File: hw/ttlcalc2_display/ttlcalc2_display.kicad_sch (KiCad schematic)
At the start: 25 parts, among them J1 DISP_CONN, J2 IO_BUS, Q1 MPSA42, Q2 MPSA42, Q3 MPSA42, Q4 MPSA42, U1 74LS138, U10 74LS04, U19 74LS04, U2 74LS138, U3 74LS173, U4 74LS173, U5 74LS173, U6 74LS08, U7 74LS173

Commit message: Display driver geographical reannotate
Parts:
- renumbered H6 to H4, H4 to H6, J2 to J4, Q2 to Q1, Q1 to Q10, Q4 to Q11, Q3 to Q24, R2 to R15, R4 to R16, R1 to R35, R3 to R36, U3 to U1, U19 to U13, U1 to U16, U6 to U17, U7 to U18, U4 to U19, U5 to U4, U10 to U5, U2 to U9
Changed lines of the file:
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@@
 		(dnp no)
 		(fields_autoplaced yes)
-		(property "Reference" "U7"
+		(property "Reference" "U18"
 			(at 270.1641 118.11 0)
 			(effects
@@
 			(project "ttlcalc2_display"
 				(path "/4da693c8-a60c-4d11-a405-739e88984bfc"
-					(reference "U7")
+					(reference "U18")
 					(unit 1)
 				)
@@
 		(dnp no)
 		(fields_autoplaced yes)
-		(property "Reference" "U3"
+		(property "Reference" "U1"
 			(at 169.8341 26.67 0)
 			(effects
@@
 			(project "ttlcalc2_display"
 				(path "/4da693c8-a60c-4d11-a405-739e88984bfc"
-					(reference "U3")
+					(reference "U1")
 					(unit 1)
 				)
@@
 		(dnp no)
 		(fields_autoplaced yes)
-		(property "Reference" "U6"
+		(property "Reference" "U17"
 			(at 245.1017 44.45 0)
 			(effects
@@
 			(project ""
 				(path "/4da693c8-a60c-4d11-a405-739e88984bfc"
-					(reference "U6")
+					(reference "U17")
 					(unit 1)
 				)
@@
 		(dnp no)
 		(fields_autoplaced yes)
-		(property "Reference" "U19"
+		(property "Reference" "U13"
 			(at 78.74 220.98 0)
 			(effects
@@
 			(project "ttlcalc2_display"
 				(path "/4da693c8-a60c-4d11-a405-739e88984bfc"
-					(reference "U19")
+					(reference "U13")
 					(unit 4)
 				)
@@
 		(dnp no)
 		(fields_autoplaced yes)
-		(property "Reference" "R4"
+		(property "Reference" "R16"
 			(at 280.67 227.33 90)
 			(effects
@@
 			(project "ttlcalc2_display"
 				(path "/4da693c8-a60c-4d11-a405-739e88984bfc"
-					(reference "R4")
+					(reference "R16")
 					(unit 1)
 				)
@@
 		(dnp no)
 		(fields_autoplaced yes)
-		(property "Reference" "R2"
+		(property "Reference" "R15"
 			(at 280.67 186.69 90)
 			(effects
@@
 			(project "ttlcalc2_display"
 				(path "/4da693c8-a60c-4d11-a405-739e88984bfc"
-					(reference "R2")
+					(reference "R15")
 					(unit 1)
 				)
@@
 		(dnp no)
 		(fields_autoplaced yes)
-		(property "Reference" "U2"
+		(property "Reference" "U9"
 			(at 111.4141 133.35 0)
 			(effects
@@
 			(project "ttlcalc2_display"
 				(path "/4da693c8-a60c-4d11-a405-739e88984bfc"
-					(reference "U2")
+					(reference "U9")
 					(unit 1)
 				)
@@
 		(dnp no)
 		(fields_autoplaced yes)
-		(property "Reference" "U6"
+		(property "Reference" "U17"
 			(at 383.5317 193.04 0)
 			(effects
@@
 			(project "ttlcalc2_display"
 				(path "/4da693c8-a60c-4d11-a405-739e88984bfc"
-					(reference "U6")
+					(reference "U17")
 					(unit 4)
 				)
@@
 		(dnp no)
 		(fields_autoplaced yes)
-		(property "Reference" "U10"
+		(property "Reference" "U5"
 			(at 45.72 220.98 0)
 			(effects
@@
 			(project "ttlcalc2_display"
 				(path "/4da693c8-a60c-4d11-a405-739e88984bfc"
-					(reference "U10")
+					(reference "U5")
 					(unit 6)
 				)
@@
 		(dnp no)
 		(fields_autoplaced yes)
-		(property "Reference" "Q2"
+		(property "Reference" "Q1"
 			(at 295.91 191.7699 0)
 			(effects
@@
 			(project "ttlcalc2_display"
 				(path "/4da693c8-a60c-4d11-a405-739e88984bfc"
-					(reference "Q2")
+					(reference "Q1")
 					(unit 1)
 				)
@@
 		(dnp no)
 		(fields_autoplaced yes)
-		(property "Reference" "U1"
+		(property "Reference" "U16"
 			(at 51.7241 133.35 0)
 			(effects
@@
 			(project "ttlcalc2_display"
 				(path "/4da693c8-a60c-4d11-a405-739e88984bfc"
-					(reference "U1")
+					(reference "U16")
 					(unit 1)
 				)
@@
 		(dnp no)
 		(fields_autoplaced yes)
-		(property "Reference" "U19"
+		(property "Reference" "U13"
 			(at 78.74 205.74 0)
 			(effects
@@
 			(project "ttlcalc2_display"
 				(path "/4da693c8-a60c-4d11-a405-739e88984bfc"
-					(reference "U19")
+					(reference "U13")
 					(unit 3)
 				)
@@
 		(dnp no)
 		(fields_autoplaced yes)
-		(property "Reference" "U6"
+		(property "Reference" "U17"
 			(at 245.1017 59.69 0)
 			(effects
@@
 			(project ""
 				(path "/4da693c8-a60c-4d11-a405-739e88984bfc"
-					(reference "U6")
+					(reference "U17")
 					(unit 2)
 				)
@@
 		(dnp no)
 		(fields_autoplaced yes)
-		(property "Reference" "U10"
+		(property "Reference" "U5"
 			(at 45.72 205.74 0)
 			(effects
@@
 			(project "ttlcalc2_display"
 				(path "/4da693c8-a60c-4d11-a405-739e88984bfc"
-					(reference "U10")
+					(reference "U5")
 					(unit 5)
 				)
@@
 		(dnp no)
 		(fields_autoplaced yes)
-		(property "Reference" "Q3"
+		(property "Reference" "Q24"
 			(at 295.91 212.0899 0)
 			(effects
@@
 			(project "ttlcalc2_display"
 				(path "/4da693c8-a60c-4d11-a405-739e88984bfc"
-					(reference "Q3")
+					(reference "Q24")
 					(unit 1)
 				)
@@
 		(dnp no)
 		(fields_autoplaced yes)
-		(property "Reference" "U5"
+		(property "Reference" "U4"
 			(at 219.3641 182.88 0)
 			(effects
@@
 			(project "ttlcalc2_display"
 				(path "/4da693c8-a60c-4d11-a405-739e88984bfc"
-					(reference "U5")
+					(reference "U4")
 					(unit 1)
 				)
@@
 		(dnp no)
 		(fields_autoplaced yes)
-		(property "Reference" "Q4"
+		(property "Reference" "Q11"
 			(at 295.91 232.4099 0)
 			(effects
@@
 			(project "ttlcalc2_display"
 				(path "/4da693c8-a60c-4d11-a405-739e88984bfc"
-					(reference "Q4")
+					(reference "Q11")
 					(unit 1)
 				)
@@
 		(dnp no)
 		(fields_autoplaced yes)
-		(property "Reference" "H4"
+		(property "Reference" "H6"
 			(at 271.78 251.4599 0)
 			(effects
@@
 			(project "ttlcalc2_display"
 				(path "/4da693c8-a60c-4d11-a405-739e88984bfc"
-					(reference "H4")
+					(reference "H6")
 					(unit 1)
 				)
@@
 		(dnp no)
 		(fields_autoplaced yes)
-		(property "Reference" "J2"
+		(property "Reference" "J4"
 			(at 355.6 172.72 0)
 			(effects
@@
 			(project "ttlcalc2_display"
 				(path "/4da693c8-a60c-4d11-a405-739e88984bfc"
-					(reference "J2")
+					(reference "J4")
 					(unit 1)
 				)
@@
 		(dnp no)
 		(fields_autoplaced yes)
-		(property "Reference" "U19"
+		(property "Reference" "U13"
 			(at 106.68 220.98 0)
 			(effects
@@
 			(project "ttlcalc2_display"
 				(path "/4da693c8-a60c-4d11-a405-739e88984bfc"
-					(reference "U19")
+					(reference "U13")
 					(unit 6)
 				)
@@
 		(dnp no)
 		(fields_autoplaced yes)
-		(property "Reference" "U19"
+		(property "Reference" "U13"
 			(at 106.68 205.74 0)
 			(effects
@@
 			(project "ttlcalc2_display"
 				(path "/4da693c8-a60c-4d11-a405-739e88984bfc"
-					(reference "U19")
+					(reference "U13")
 					(unit 5)
 				)
@@
 		(dnp no)
 		(fields_autoplaced yes)
-		(property "Reference" "U4"
+		(property "Reference" "U19"
 			(at 218.0941 74.93 0)
 			(effects
@@
 			(project "ttlcalc2_display"
 				(path "/4da693c8-a60c-4d11-a405-739e88984bfc"
-					(reference "U4")
+					(reference "U19")
 					(unit 1)
 				)
@@
 		(dnp no)
 		(fields_autoplaced yes)
-		(property "Reference" "R1"
+		(property "Reference" "R35"
 			(at 280.67 166.37 90)
 			(effects
@@
 			(project "ttlcalc2_display"
 				(path "/4da693c8-a60c-4d11-a405-739e88984bfc"
-					(reference "R1")
+					(reference "R35")
 					(unit 1)
 				)
@@
 		(dnp no)
 		(fields_autoplaced yes)
-		(property "Reference" "H6"
+		(property "Reference" "H4"
 			(at 290.83 251.4599 0)
 			(effects
@@
 			(project "ttlcalc2_display"
 				(path "/4da693c8-a60c-4d11-a405-739e88984bfc"
-					(reference "H6")
+					(reference "H4")
 					(unit 1)
 				)
@@
 		(dnp no)
 		(fields_autoplaced yes)
-		(property "Reference" "U6"
+		(property "Reference" "U17"
 			(at 264.1517 52.07 0)
 			(effects
@@
 			(project ""
 				(path "/4da693c8-a60c-4d11-a405-739e88984bfc"
-					(reference "U6")
+					(reference "U17")
 					(unit 3)
 				)
@@
 		(dnp no)
 		(fields_autoplaced yes)
-		(property "Reference" "Q1"
+		(property "Reference" "Q10"
 			(at 295.91 171.4499 0)
 			(effects
@@
 			(project "ttlcalc2_display"
 				(path "/4da693c8-a60c-4d11-a405-739e88984bfc"
-					(reference "Q1")
+					(reference "Q10")
 					(unit 1)
 				)
@@
 		(dnp no)
 		(fields_autoplaced yes)
-		(property "Reference" "R3"
+		(property "Reference" "R36"
 			(at 280.67 207.01 90)
 			(effects
@@
 			(project "ttlcalc2_display"
 				(path "/4da693c8-a60c-4d11-a405-739e88984bfc"
-					(reference "R3")
+					(reference "R36")
 					(unit 1)
 				)

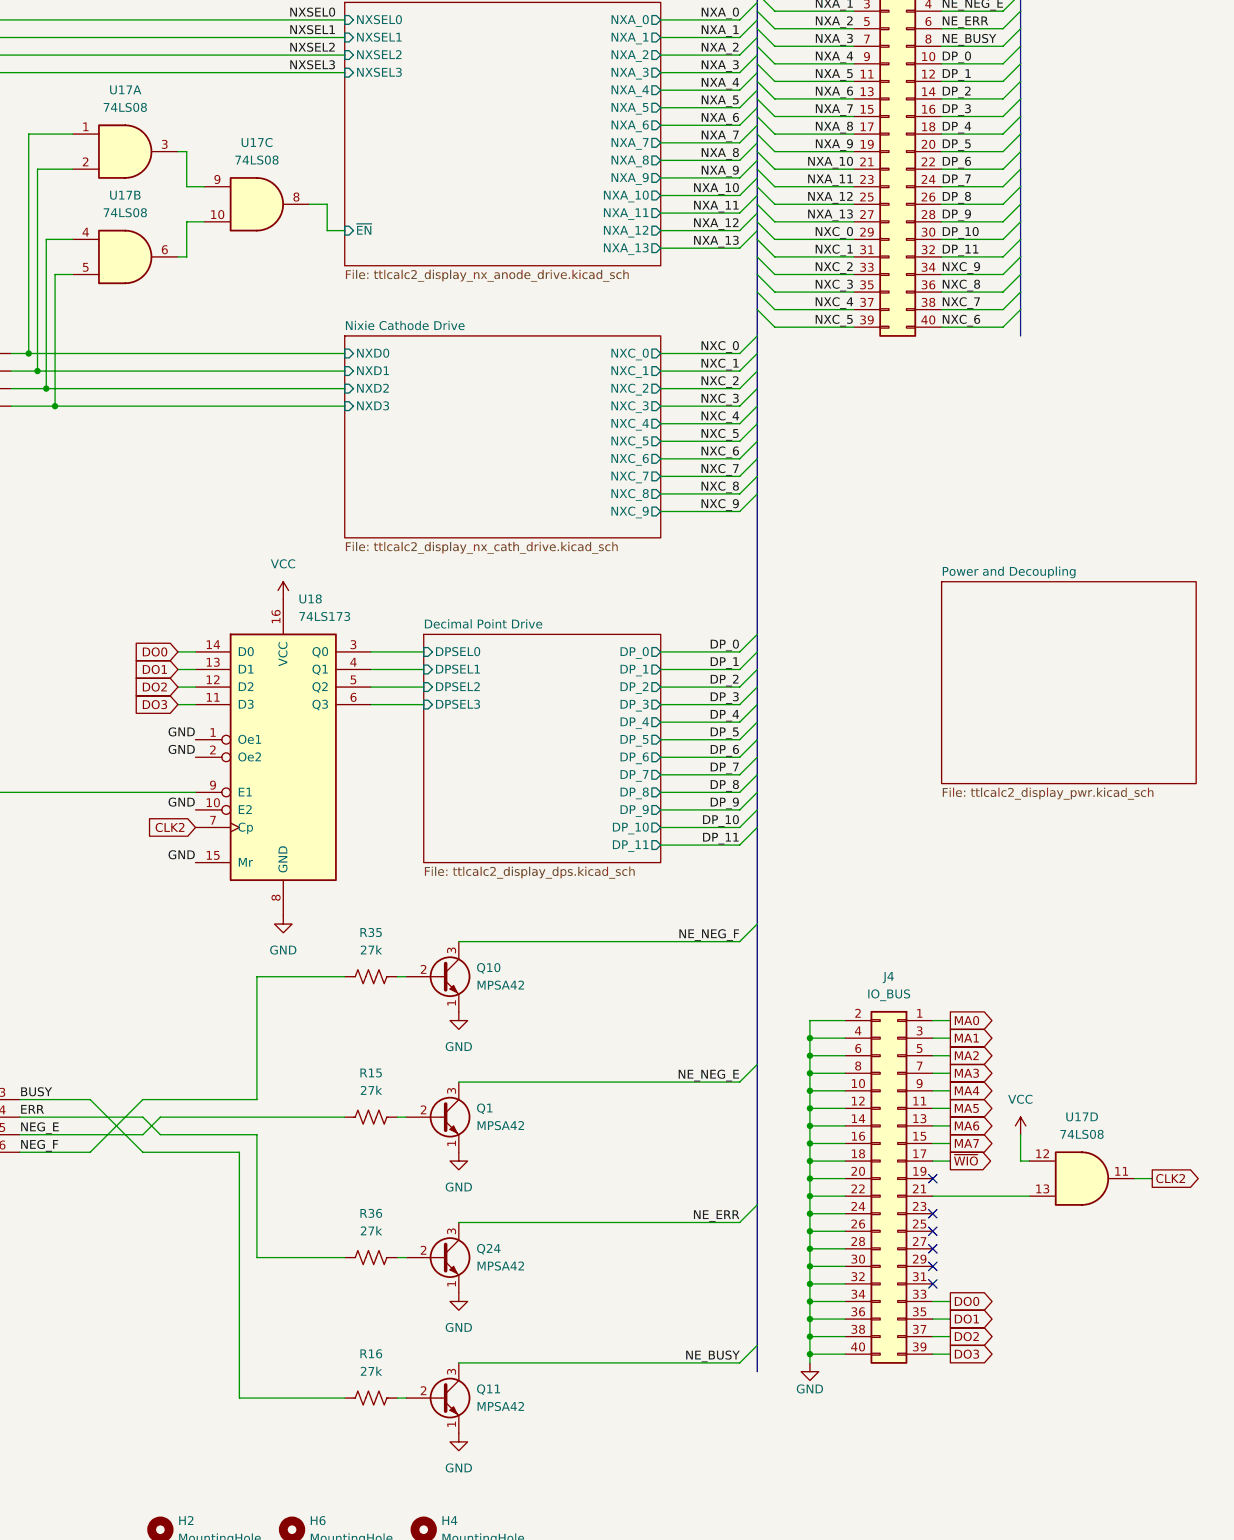
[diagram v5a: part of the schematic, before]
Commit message: Convert to KiCad 9.0
Convert to KiCad 9.0 format
Tweak silkscreen to fix DRC errors introduced by updated footprints
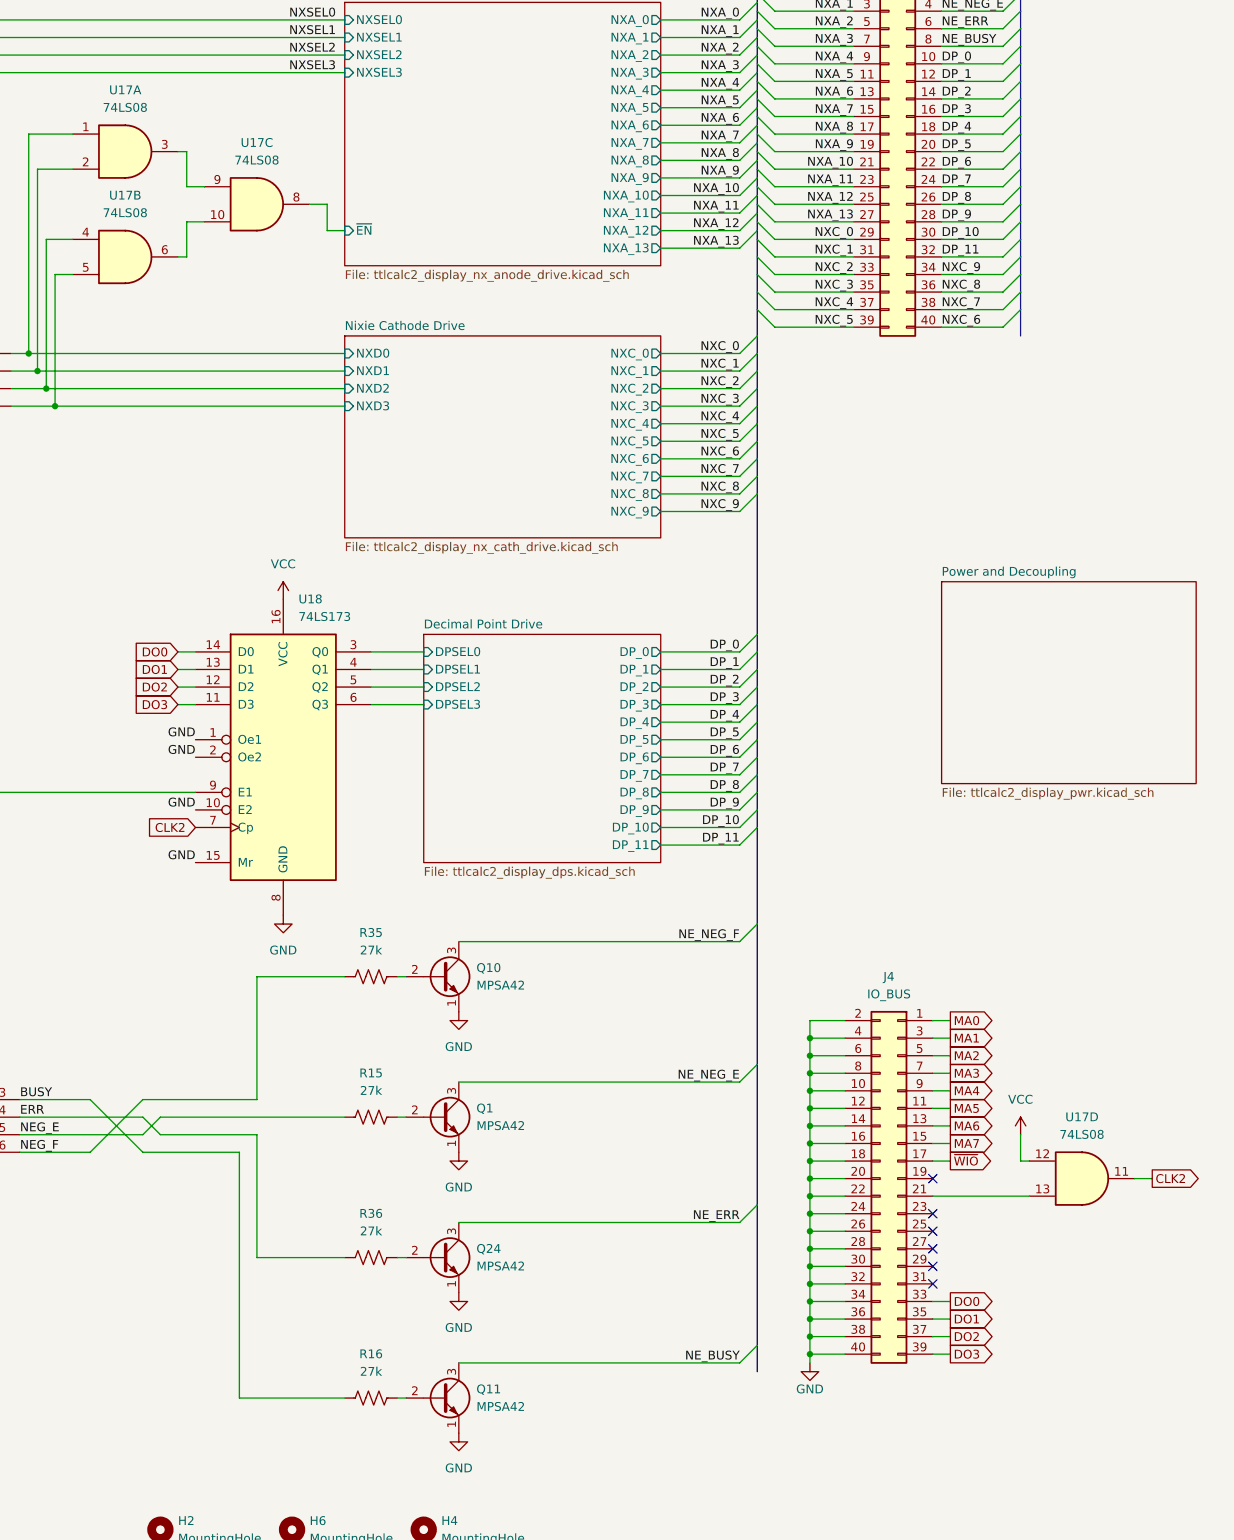
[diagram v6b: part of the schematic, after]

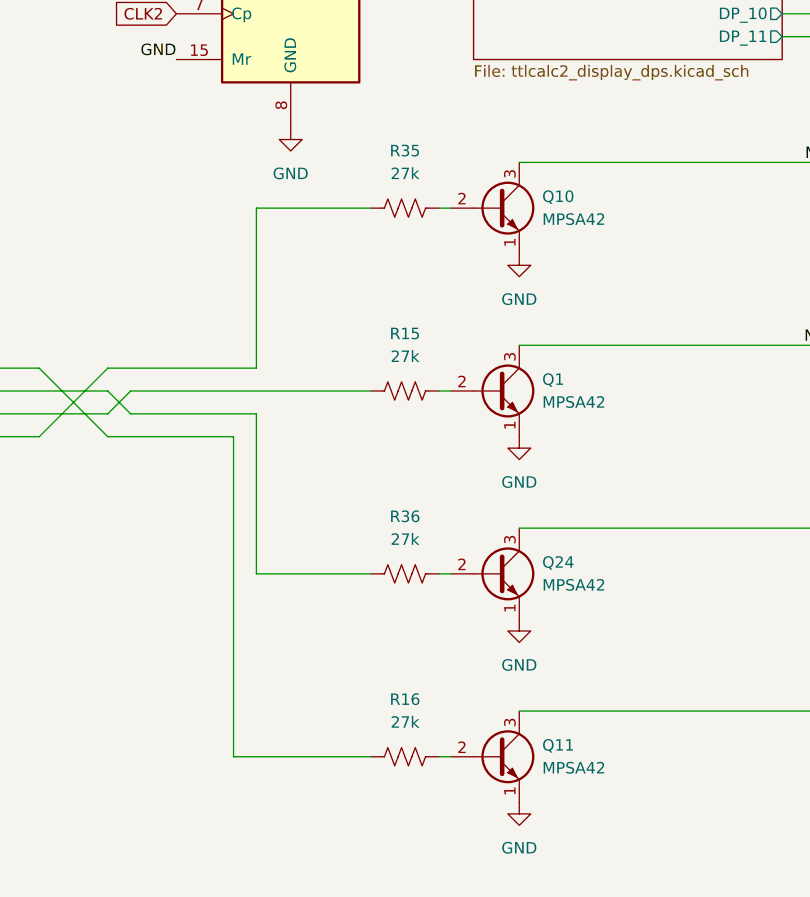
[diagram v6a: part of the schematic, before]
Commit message: Minor display hardware revisions
Add anti-ghosting inter-cathode resistors to nixies
Adjust component values based on experiments
Change from individual netclass labels to rule areas
Tweak traces on display board
Update .gitignore to ignore KiCad lock files
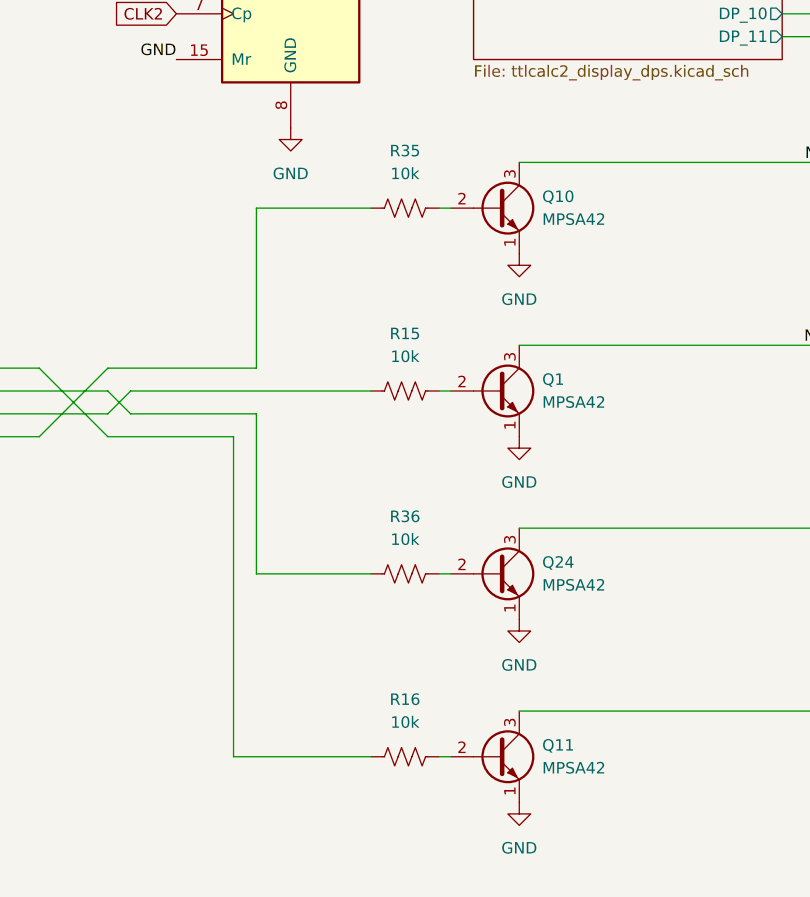
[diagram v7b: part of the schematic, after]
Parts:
- R15, R16, R35, R36: value 27k -> 10k
